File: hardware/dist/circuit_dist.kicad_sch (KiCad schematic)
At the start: 27 parts, among them U7 TL072

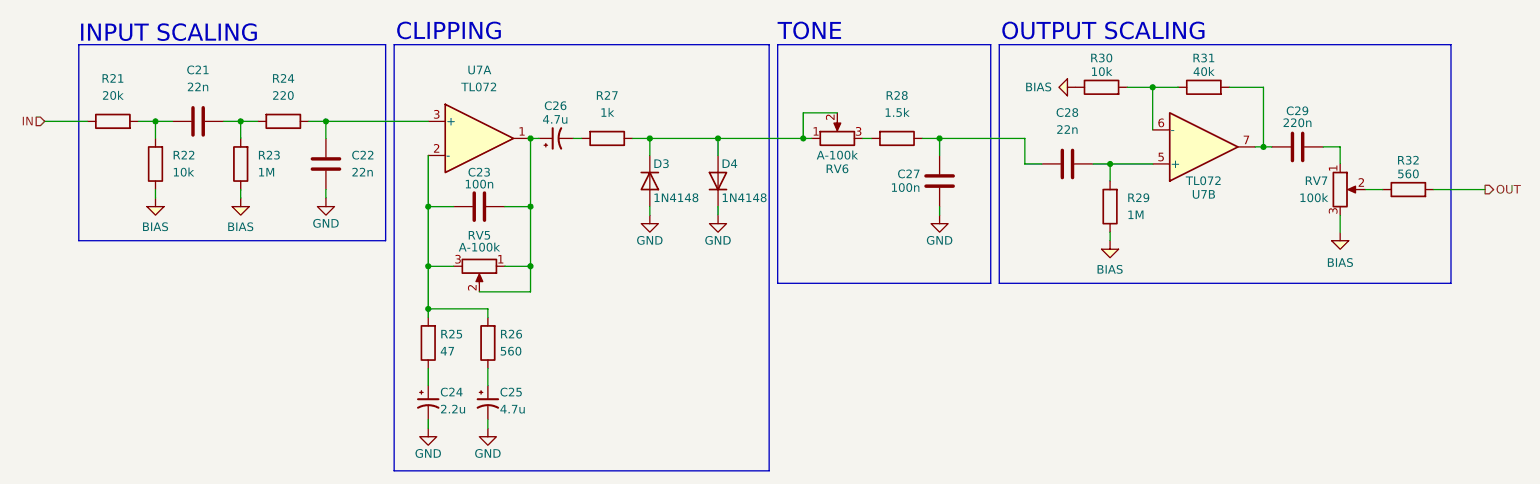
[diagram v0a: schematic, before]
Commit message: bom + kicad fix for dual supply
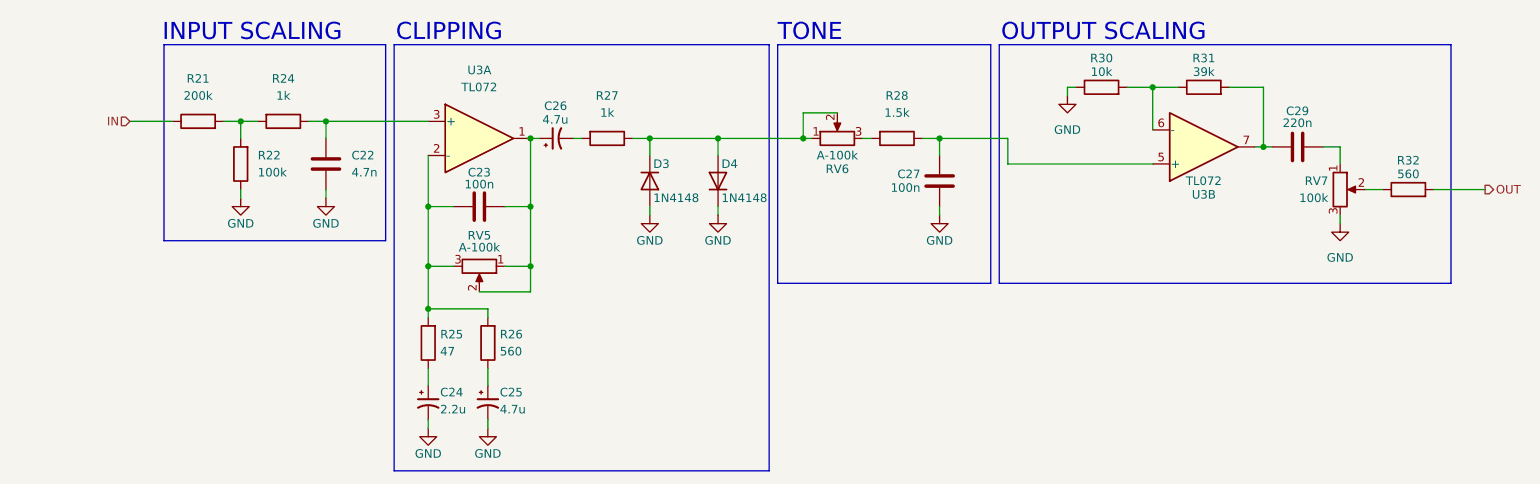
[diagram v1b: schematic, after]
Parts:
- removed C21, C28: 22n, symbol Device:C
- removed R23, R29: 1M, symbol Device:R
- C22: value 22n -> 4.7n; footprint (none) -> Capacitor_SMD:C_0402_1005Metric
- C23, C27, C29: footprint (none) -> Capacitor_SMD:C_0402_1005Metric
- C24, C25, C26: footprint (none) -> Capacitor_THT:CP_Radial_D4.0mm_P1.50mm
- D3, D4: footprint Diode_THT:D_DO-35_SOD27_P7.62mm_Horizontal -> Diode_SMD:D_SOD-323
- R21: value 20k -> 200k; footprint (none) -> Resistor_SMD:R_0402_1005Metric
- R22: value 10k -> 100k; footprint (none) -> Resistor_SMD:R_0402_1005Metric
- R24: value 220 -> 1k; footprint (none) -> Resistor_SMD:R_0402_1005Metric
- R25, R26, R27, R28, R30, R32: footprint (none) -> Resistor_SMD:R_0402_1005Metric
- R31: value 40k -> 39k; footprint (none) -> Resistor_SMD:R_0402_1005Metric
- RV5, RV6, RV7: footprint (none) -> Potentiometer_THT:Potentiometer_Alps_RK09K_Single_Vertical
- U3: renamed from U7; footprint (none) -> TL072CDT:D8_TEX_STM
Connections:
- net BIAS is gone; now on net GND: R22.1, R30.1, RV7.3
- net at C27.2, R28.1: now also U3.5 (+)
- net at R21.2, R22.2: now also R24.2
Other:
- moved on the sheet: R21, R22

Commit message: finish pcb
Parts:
- C22, C23, C27, C29: footprint Capacitor_SMD:C_0402_1005Metric -> Capacitor_SMD:C_0805_2012Metric_Pad1.18x1.45mm_HandSolder
- R21, R22, R24, R25, R26, R27, R28, R30, R31, R32: footprint Resistor_SMD:R_0402_1005Metric -> Resistor_SMD:R_0805_2012Metric_Pad1.20x1.40mm_HandSolder
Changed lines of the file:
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@@
 			)
 		)
-		(property "Footprint" "Capacitor_SMD:C_0402_1005Metric"
+		(property "Footprint" "Capacitor_SMD:C_0805_2012Metric_Pad1.18x1.45mm_HandSolder"
 			(at 234.95 91.7448 0)
 			(hide yes)
@@
 			)
 		)
-		(property "Footprint" "Resistor_SMD:R_0402_1005Metric"
+		(property "Footprint" "Resistor_SMD:R_0805_2012Metric_Pad1.20x1.40mm_HandSolder"
 			(at 217.17 85.598 90)
 			(hide yes)
@@
 			)
 		)
-		(property "Footprint" "Resistor_SMD:R_0402_1005Metric"
+		(property "Footprint" "Resistor_SMD:R_0805_2012Metric_Pad1.20x1.40mm_HandSolder"
 			(at 201.93 85.598 90)
 			(hide yes)
@@
 			)
 		)
-		(property "Footprint" "Capacitor_SMD:C_0402_1005Metric"
+		(property "Footprint" "Capacitor_SMD:C_0805_2012Metric_Pad1.18x1.45mm_HandSolder"
 			(at 113.03 100.6348 0)
 			(hide yes)
@@
 			)
 		)
-		(property "Footprint" "Resistor_SMD:R_0402_1005Metric"
+		(property "Footprint" "Resistor_SMD:R_0805_2012Metric_Pad1.20x1.40mm_HandSolder"
 			(at 112.268 121.92 90)
 			(hide yes)
@@
 			)
 		)
-		(property "Footprint" "Resistor_SMD:R_0402_1005Metric"
+		(property "Footprint" "Resistor_SMD:R_0805_2012Metric_Pad1.20x1.40mm_HandSolder"
 			(at 128.27 89.662 90)
 			(hide yes)
@@
 			)
 		)
-		(property "Footprint" "Capacitor_SMD:C_0402_1005Metric"
+		(property "Footprint" "Capacitor_SMD:C_0805_2012Metric_Pad1.18x1.45mm_HandSolder"
 			(at 85.3948 91.44 0)
 			(hide yes)
@@
 			)
 		)
-		(property "Footprint" "Resistor_SMD:R_0402_1005Metric"
+		(property "Footprint" "Resistor_SMD:R_0805_2012Metric_Pad1.20x1.40mm_HandSolder"
 			(at 75.438 95.25 90)
 			(hide yes)
@@
 			)
 		)
-		(property "Footprint" "Capacitor_SMD:C_0402_1005Metric"
+		(property "Footprint" "Capacitor_SMD:C_0805_2012Metric_Pad1.18x1.45mm_HandSolder"
 			(at 176.8348 93.98 0)
 			(hide yes)
@@
 			)
 		)
-		(property "Footprint" "Resistor_SMD:R_0402_1005Metric"
+		(property "Footprint" "Resistor_SMD:R_0805_2012Metric_Pad1.20x1.40mm_HandSolder"
 			(at 171.45 89.662 90)
 			(hide yes)
@@
 			)
 		)
-		(property "Footprint" "Resistor_SMD:R_0402_1005Metric"
+		(property "Footprint" "Resistor_SMD:R_0805_2012Metric_Pad1.20x1.40mm_HandSolder"
 			(at 247.65 100.838 90)
 			(hide yes)
@@
 			)
 		)
-		(property "Footprint" "Resistor_SMD:R_0402_1005Metric"
+		(property "Footprint" "Resistor_SMD:R_0805_2012Metric_Pad1.20x1.40mm_HandSolder"
 			(at 80.01 87.122 90)
 			(hide yes)
@@
 			)
 		)
-		(property "Footprint" "Resistor_SMD:R_0402_1005Metric"
+		(property "Footprint" "Resistor_SMD:R_0805_2012Metric_Pad1.20x1.40mm_HandSolder"
 			(at 67.31 90.678 90)
 			(hide yes)
@@
 			)
 		)
-		(property "Footprint" "Resistor_SMD:R_0402_1005Metric"
+		(property "Footprint" "Resistor_SMD:R_0805_2012Metric_Pad1.20x1.40mm_HandSolder"
 			(at 103.378 121.92 90)
 			(hide yes)
